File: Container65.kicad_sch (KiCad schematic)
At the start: 97 parts, among them J1 Conn_01x03, J3 POGOm1, J4 POGOm2, J5 POGOf1, J6 POGOf2, SW1 RotaryEncoder_Switch, U1 RP2040, U2 TYPE-C-31-M-12, U3 XC6206PxxxMR, U4 W25Q128JVS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

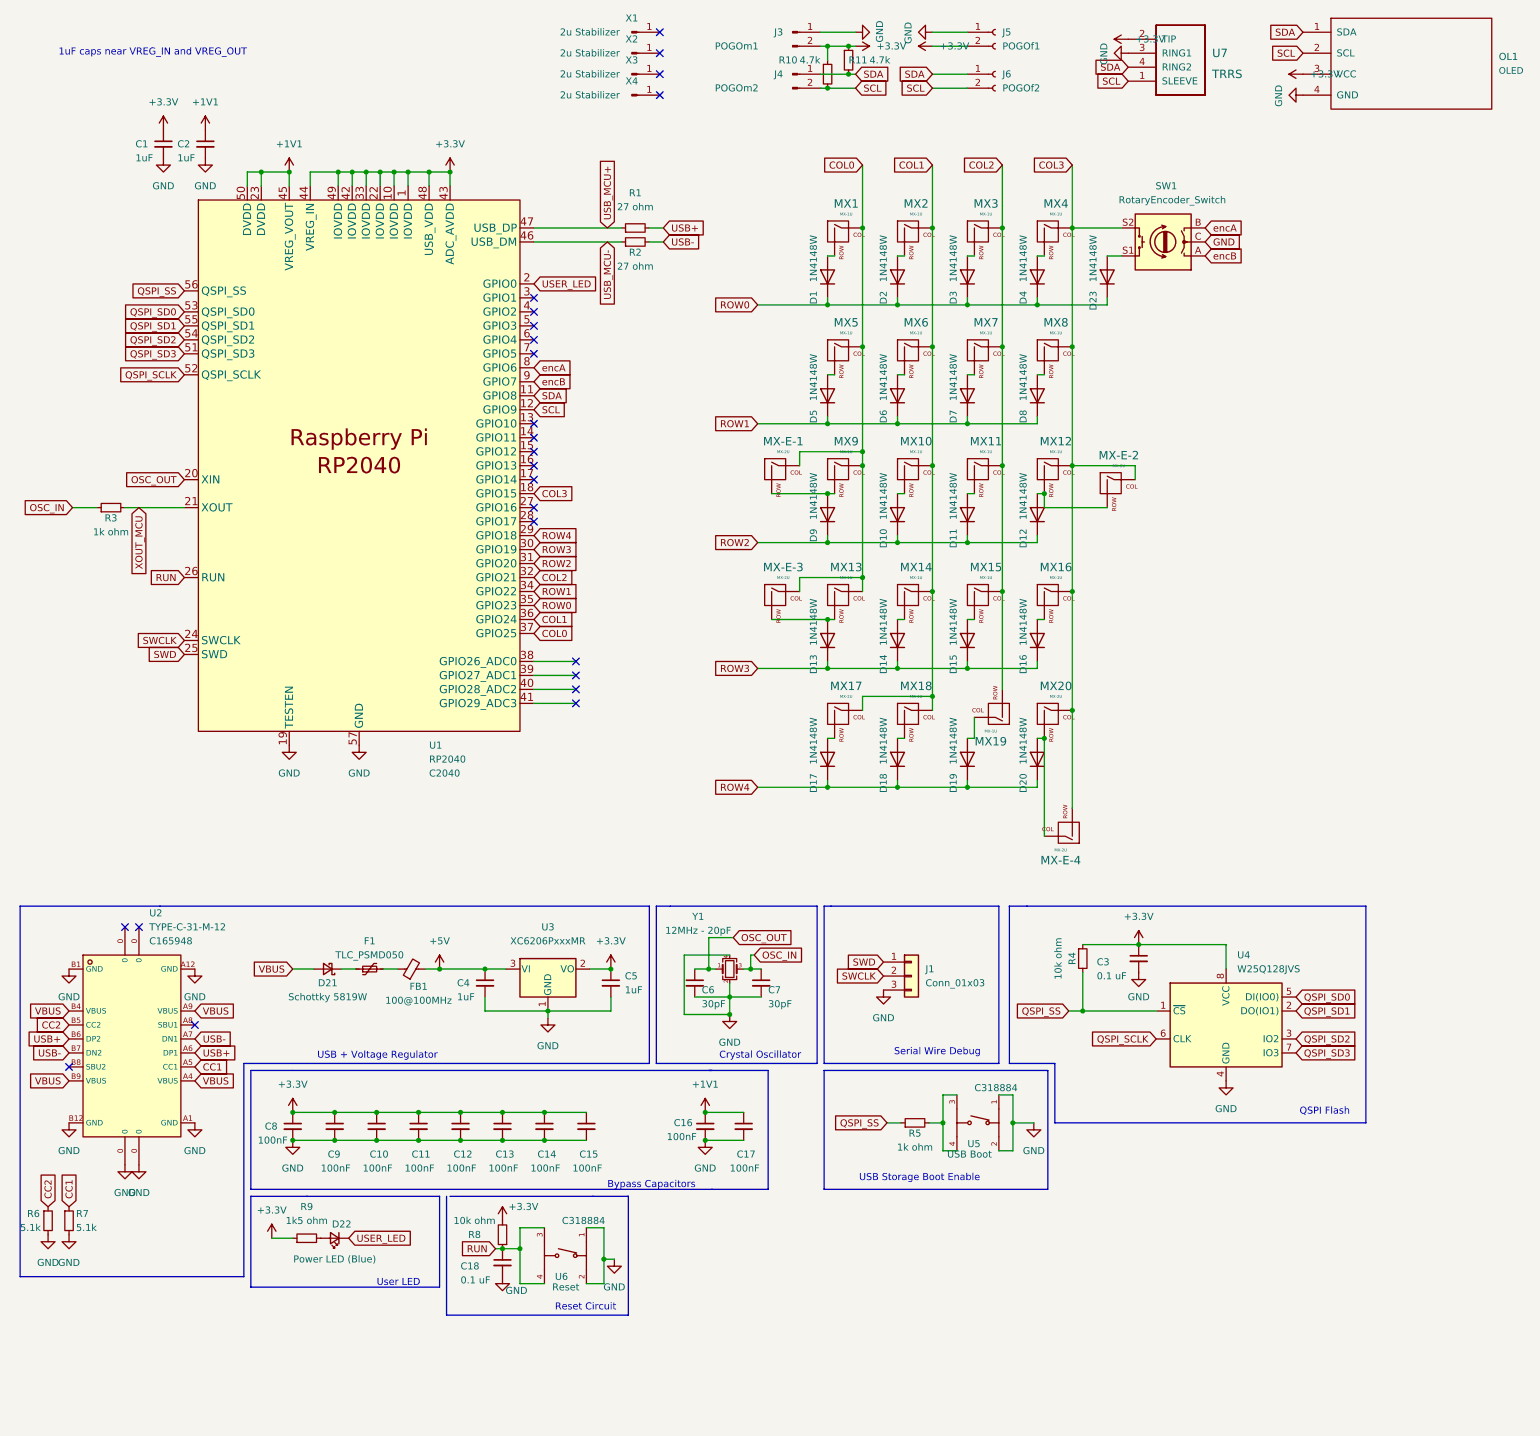
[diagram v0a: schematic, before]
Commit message: Add eblaster lib
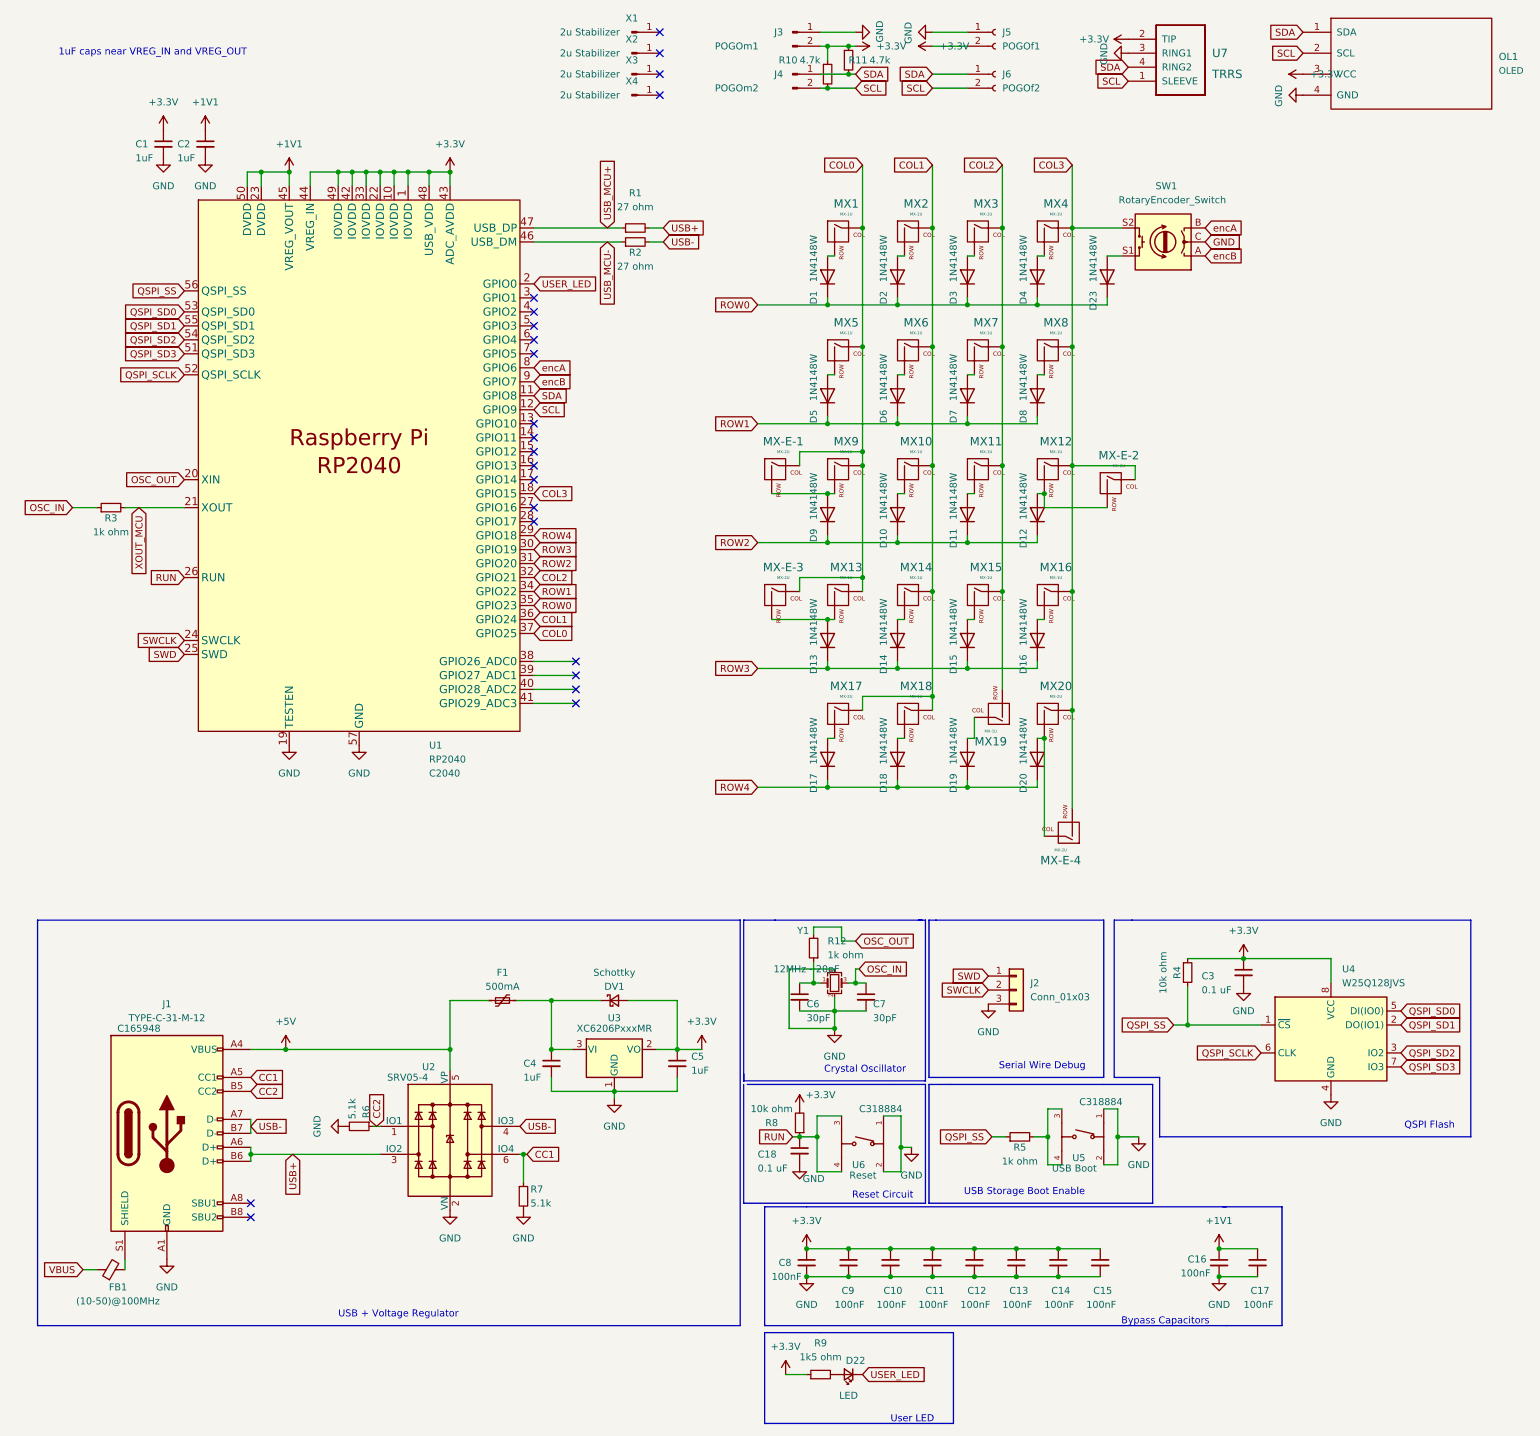
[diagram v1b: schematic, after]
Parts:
- removed D21: Schottky 5819W, Keebio-Parts:D_SOD123, symbol Device:D_Schottky_Small
- removed U2: TYPE-C-31-M-12, Extras:simple-usb-c, symbol simple-usb-c:TYPE-C-31-M-12
- added DV1: Schottky, Fuse:Fuse_1206_3216Metric, symbol Device:D_Schottky_Small
- added J1: TYPE-C-31-M-12, Keebio-Parts:HRO-TYPE-C-31-M-12-Assembly, symbol Connector:USB_C_Receptacle_USB2.0
- added R12: 1k ohm, Keebio-Parts:R_0402, symbol Device:R_Small
- added U2: SRV05-4, Package_TO_SOT_SMD:SOT-23-6, symbol Power_Protection:SRV05-4
- D22: value Power LED (Blue) -> LED
- F1: value TLC_PSMD050 -> 500mA; Part (none) -> TLC_PSMD050
- FB1: value 100@100MHz -> (10-50)@100MHz
- J2: renamed from J1; now left out of the parts list
- U1: footprint Extras:rp2040 -> Keebio-Parts:RP2040-QFN-56
- U5, U6: footprint Extras:3x4x2.5mm Micro Switch -> Extras:tactile-switch
- X1, X2, X3, X4: now left out of the parts list
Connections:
- net +3V3: now also DV1.2 (A)
- net +5V: now also F1.1, J1.A4 (VBUS), J1.A9 (VBUS), J1.B4 (VBUS), J1.B9 (VBUS), U2.5 (VP); no longer C4.1, FB1.2, U3.3 (VI)
- net CC1: now also J1.A5 (CC1), U2.6 (IO4)
- net CC2: now also J1.B5 (CC2), U2.1 (IO1)
- net GND: now also J1.A1 (GND), J1.A12 (GND), J1.B1 (GND), J1.B12 (GND), U2.2 (VN)
- net OSC_OUT: now also R12.2; no longer C6.1, Y1.1
- net USB+: now also J1.A6 (D+), J1.B6 (D+), U2.3 (IO2)
- net USB-: now also J1.A7 (D-), J1.B7 (D-), U2.4 (IO3)
- net VBUS: now also FB1.1
- net at F1.2: now also C4.1, U3.3 (VI), DV1.1 (K); no longer FB1.1
- new net: FB1.2, J1.S1 (SHIELD)
- new net: C6.1, R12.1, Y1.1
- no-connect marks 24 -> 22
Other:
- moved on the sheet: C10, C11, C12, C13, C14, C15, C16, C17, C18, C3, C6, C7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
